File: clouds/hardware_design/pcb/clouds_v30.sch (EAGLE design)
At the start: 155 parts, among them IC1 74HC595D, IC10 TL072D, IC2 LM1117-3.3, IC3 MCP6002, IC4 MCP6004, IC5 STM32F405RGT6, IC6 LM4040B10, IC7 LM1117-3.3, IC8 WM8731, IC9 TL072D, J1 PJ301_THONKICONN6, J10 PJ301_THONKICONN6, J11 PJ301_THONKICONN6, J12 PJ301_THONKICONN6, J2 PJ301_THONKICONN6, J3 PJ301_THONKICONN6, J4 PJ301_THONKICONN6, J5 PJ301_THONKICONN6, J6 PJ301_THONKICONN6, J7 PJ301_THONKICONN6, J8 PJ301_THONKICONN6, J9 PJ301_THONKICONN6, Q1 MMBT3904, Q2 MMBT3904, Q3 8MHz, Q4 12.288MHz, SW1 LP4OA1PBCT, SW4 EVQQ2, SW5 EVQQ2

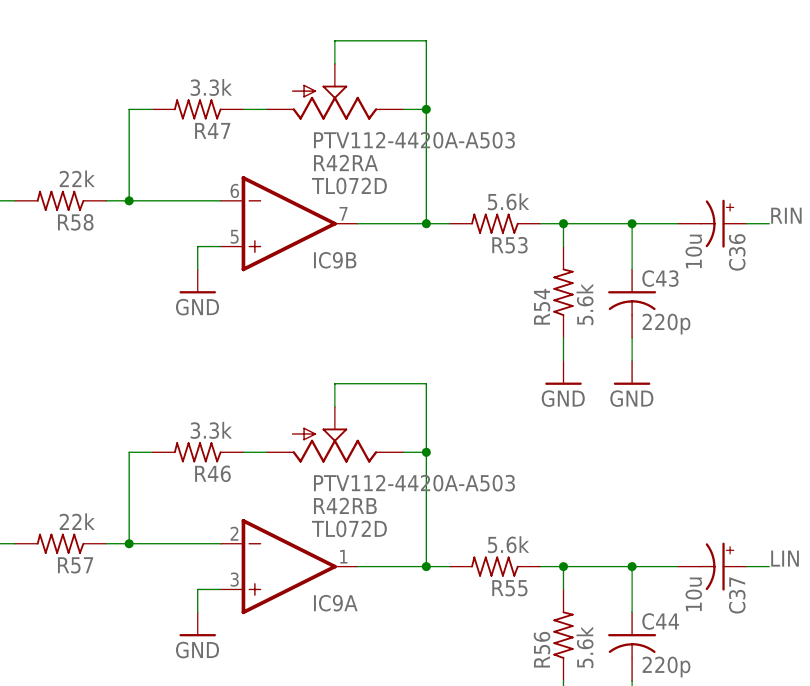
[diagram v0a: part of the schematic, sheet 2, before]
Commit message: convert R42 from BOURNS_PTV112 to ALPHA_RD902F-040
Signed-off-by: vladimir <vladimir@pantelic.net>
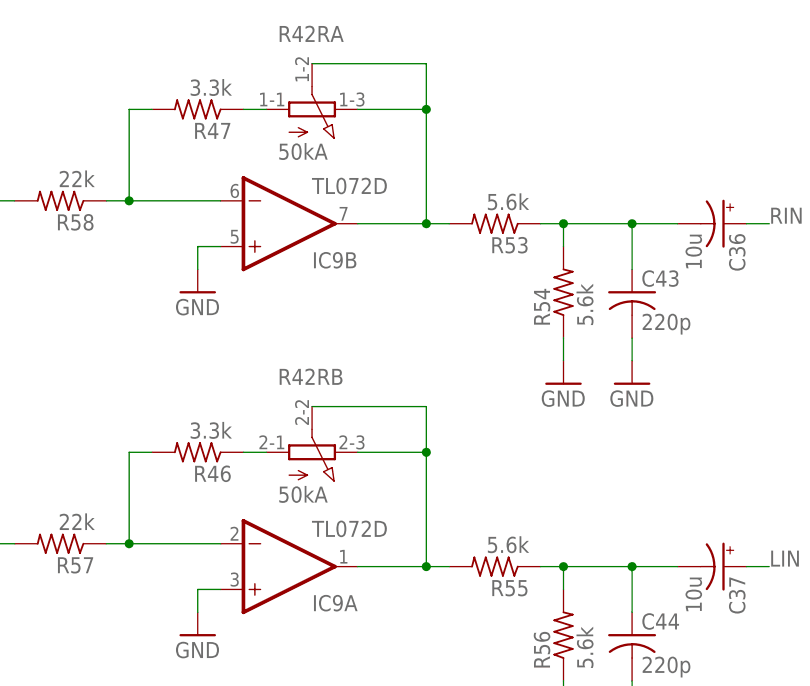
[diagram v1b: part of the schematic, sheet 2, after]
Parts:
- R42: value PTV112-4420A-A503 -> 50kA; device og-pots:POT_US_DUAL_GANG -> 00vp:RD902F-040
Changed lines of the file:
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@@
 <part name="SUPPLY4" library="supply2" deviceset="VEE" device=""/>
 <part name="P+1" library="SparkFun" deviceset="VCC" device=""/>
-<part name="R42" library="og-pots" deviceset="POT_US_DUAL_GANG" device="" value="PTV112-4420A-A503"/>
 <part name="R47" library="rcl" deviceset="R-US_" device="R0603" value="3.3k"/>
 <part name="R46" library="rcl" deviceset="R-US_" device="R0603" value="3.3k"/>
@@
 <part name="R11" library="rcl" deviceset="R-US_" device="R1206" value="4.7"/>
 <part name="GND72" library="SparkFun" deviceset="GND" device=""/>
+<part name="R42" library="00vp" deviceset="RD902F-040" device="" value="50kA"/>
 </parts>
 <sheets>
@@
 <instance part="SUPPLY4" gate="G$1" x="109.22" y="38.1" rot="R180"/>
 <instance part="P+1" gate="1" x="109.22" y="71.12"/>
-<instance part="R42" gate="RA" x="-66.04" y="86.36" rot="MR90"/>
-<instance part="R42" gate="RB" x="-66.04" y="48.26" rot="MR90"/>
 <instance part="R47" gate="G$1" x="-81.28" y="86.36" rot="R180"/>
 <instance part="R46" gate="G$1" x="-81.28" y="48.26" rot="R180"/>
@@
 <instance part="J4" gate="G$1" x="-50.8" y="-96.52" rot="MR0"/>
 <instance part="J10" gate="G$1" x="15.24" y="-96.52" rot="MR0"/>
+<instance part="R42" gate="RA" x="-68.58" y="86.36" smashed="yes" rot="MR90">
+<attribute name="NAME" x="-72.39" y="95.631" size="1.778" layer="95" rot="MR180"/>
+<attribute name="VALUE" x="-72.39" y="82.55" size="1.778" layer="96" rot="MR180"/>
+</instance>
+<instance part="R42" gate="RB" x="-68.58" y="48.26" smashed="yes" rot="MR90">
+<attribute name="NAME" x="-72.39" y="57.531" size="1.778" layer="95" rot="MR180"/>
+<attribute name="VALUE" x="-72.39" y="44.45" size="1.778" layer="96" rot="MR180"/>
+</instance>
 </instances>
 <busses>
@@
 <net name="N$42" class="0">
 <segment>
-<wire x1="-66.04" y1="91.44" x2="-66.04" y2="93.98" width="0.1524" layer="91"/>
-<wire x1="-66.04" y1="93.98" x2="-55.88" y2="93.98" width="0.1524" layer="91"/>
-<wire x1="-55.88" y1="93.98" x2="-55.88" y2="86.36" width="0.1524" layer="91"/>
-<wire x1="-55.88" y1="86.36" x2="-58.42" y2="86.36" width="0.1524" layer="91"/>
-<wire x1="-55.88" y1="86.36" x2="-55.88" y2="73.66" width="0.1524" layer="91"/>
 <wire x1="-55.88" y1="73.66" x2="-63.5" y2="73.66" width="0.1524" layer="91"/>
 <wire x1="-55.88" y1="73.66" x2="-53.34" y2="73.66" width="0.1524" layer="91"/>
-<junction x="-55.88" y="86.36"/>
 <junction x="-55.88" y="73.66"/>
-<pinref part="R42" gate="RA" pin="S"/>
-<pinref part="R42" gate="RA" pin="E"/>
 <pinref part="IC9" gate="B" pin="OUT"/>
 <pinref part="R53" gate="G$1" pin="2"/>
+<pinref part="R42" gate="RA" pin="S"/>
+<wire x1="-68.58" y1="91.44" x2="-55.88" y2="91.44" width="0.1524" layer="91"/>
+<wire x1="-55.88" y1="91.44" x2="-55.88" y2="86.36" width="0.1524" layer="91"/>
+<pinref part="R42" gate="RA" pin="E"/>
+<wire x1="-63.5" y1="86.36" x2="-55.88" y2="86.36" width="0.1524" layer="91"/>
+<wire x1="-55.88" y1="86.36" x2="-55.88" y2="73.66" width="0.1524" layer="91"/>
+<junction x="-55.88" y="86.36"/>
 </segment>
 </net>
 <net name="N$51" class="0">
 <segment>
-<wire x1="-66.04" y1="53.34" x2="-66.04" y2="55.88" width="0.1524" layer="91"/>
-<wire x1="-66.04" y1="55.88" x2="-55.88" y2="55.88" width="0.1524" layer="91"/>
-<wire x1="-55.88" y1="55.88" x2="-55.88" y2="48.26" width="0.1524" layer="91"/>
-<wire x1="-55.88" y1="48.26" x2="-58.42" y2="48.26" width="0.1524" layer="91"/>
 <wire x1="-55.88" y1="48.26" x2="-55.88" y2="35.56" width="0.1524" layer="91"/>
 <wire x1="-55.88" y1="35.56" x2="-63.5" y2="35.56" width="0.1524" layer="91"/>
 <wire x1="-55.88" y1="35.56" x2="-53.34" y2="35.56" width="0.1524" layer="91"/>
-<junction x="-55.88" y="48.26"/>
 <junction x="-55.88" y="35.56"/>
-<pinref part="R42" gate="RB" pin="S"/>
-<pinref part="R42" gate="RB" pin="E"/>
 <pinref part="IC9" gate="A" pin="OUT"/>
 <pinref part="R55" gate="G$1" pin="2"/>
+<pinref part="R42" gate="RB" pin="E"/>
+<wire x1="-55.88" y1="48.26" x2="-63.5" y2="48.26" width="0.1524" layer="91"/>
+<pinref part="R42" gate="RB" pin="S"/>
+<wire x1="-68.58" y1="53.34" x2="-55.88" y2="53.34" width="0.1524" layer="91"/>
+<wire x1="-55.88" y1="53.34" x2="-55.88" y2="48.26" width="0.1524" layer="91"/>
+<junction x="-55.88" y="48.26"/>
 </segment>
 </net>
@@
 <net name="N$53" class="0">
 <segment>
-<wire x1="-76.2" y1="48.26" x2="-73.66" y2="48.26" width="0.1524" layer="91"/>
 <pinref part="R46" gate="G$1" pin="1"/>
 <pinref part="R42" gate="RB" pin="A"/>
-</segment>
-</net>
+<wire x1="-73.66" y1="48.26" x2="-76.2" y2="48.26" width="0.1524" layer="91"/>
+</segment>
+</net>
